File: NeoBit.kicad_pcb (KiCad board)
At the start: 2 copper layers, 67.3 x 45.7 mm, 13 parts, among them J2 Barrel_Jack_MountingPin, J4 NeoPixels, J5 microbit_edge_connector, U1 74AHCT125, U2 MCP1702-3302E_TO92

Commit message: Wire things up.
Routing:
- net +3V3: track 0.00 -> 99.5 mm, vias 0 -> 1
- net Net-(R2-Pad1): track 0.00 -> 90.5 mm, vias 0 -> 2
- net /P2: track 0.00 -> 69.6 mm, vias 0 -> 1
- net /P0: track 0.00 -> 46.3 mm, vias 0 -> 2
- net /P1: track 0.00 -> 33.6 mm, vias 0 -> 1
- net +5V: track 0.00 -> 33.5 mm
- net Net-(C4-Pad1): track 0.00 -> 8.41 mm
- net Net-(J4-Pad1): track 0.00 -> 6.02 mm
- added copper zone on F.Cu, net +5V
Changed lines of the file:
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@@
     (thickness 1.6)
     (drawings 8)
-    (tracks 0)
+    (tracks 84)
     (zones 0)
     (modules 13)
@@
     (pad_to_mask_clearance 0)
     (aux_axis_origin 0 0)
-    (visible_elements FFFEF77F)
+    (visible_elements FFFEE77F)
     (pcbplotparams
       (layerselection 0x00030_80000001)
@@
   (gr_arc (start 121.285 127) (end 121.285 129.54) (angle 90) (layer Edge.Cuts) (width 0.15))
   (gr_arc (start 121.285 86.36) (end 118.745 86.36) (angle 90) (layer Edge.Cuts) (width 0.15))
+  (segment (start 140.335 114.3) (end 137.795 114.3) (width 0.508) (layer F.Cu) (net 1))
+  (segment (start 137.795 114.3) (end 136.525 115.57) (width 0.508) (layer F.Cu) (net 1))
+  (segment (start 149.86 113.03) (end 149.49401 113.39599) (width 0.508) (layer F.Cu) (net 1))
+  (segment (start 149.49401 113.39599) (end 149.49401 113.704453) (width 0.508) (layer F.Cu) (net 1))
+  (segment (start 148.898463 114.3) (end 141.46637 114.3) (width 0.508) (layer F.Cu) (net 1))
+  (segment (start 149.49401 113.704453) (end 148.898463 114.3) (width 0.508) (layer F.Cu) (net 1))
+  (segment (start 141.46637 114.3) (end 140.335 114.3) (width 0.508) (layer F.Cu) (net 1))
+  (segment (start 154.94 111.125) (end 150.507 111.125) (width 0.508) (layer F.Cu) (net 1))
+  (segment (start 150.507 111.125) (end 149.86 111.772) (width 0.508) (layer F.Cu) (net 1))
+  (segment (start 149.86 111.772) (end 149.86 113.03) (width 0.508) (layer F.Cu) (net 1))
+  (segment (start 166.37 111.76) (end 163.521922 111.76) (width 0.508) (layer F.Cu) (net 1))
+  (segment (start 163.521922 111.76) (end 162.067921 110.305999) (width 0.508) (layer F.Cu) (net 1))
+  (segment (start 162.067921 110.305999) (end 155.759001 110.305999) (width 0.508) (layer F.Cu) (net 1))
+  (segment (start 155.759001 110.305999) (end 155.739999 110.325001) (width 0.508) (layer F.Cu) (net 1))
+  (segment (start 155.739999 110.325001) (end 154.94 111.125) (width 0.508) (layer F.Cu) (net 1))
+  (segment (start 144.78 111.125) (end 144.78 107.315) (width 0.508) (layer B.Cu) (net 3))
+  (segment (start 148.59 113.03) (end 146.685 113.03) (width 0.508) (layer F.Cu) (net 3))
+  (segment (start 146.685 113.03) (end 144.78 111.125) (width 0.508) (layer F.Cu) (net 3))
+  (segment (start 179.15 121.92) (end 183.609001 117.460999) (width 0.508) (layer B.Cu) (net 4))
+  (segment (start 183.609001 117.460999) (end 183.609001 106.089923) (width 0.508) (layer B.Cu) (net 4))
+  (segment (start 183.609001 106.089923) (end 179.15 101.630922) (width 0.508) (layer B.Cu) (net 4))
+  (segment (start 179.15 101.630922) (end 179.15 99.345634) (width 0.508) (layer B.Cu) (net 4))
+  (segment (start 179.15 99.345634) (end 179.15 97.79) (width 0.508) (layer B.Cu) (net 4))
+  (segment (start 157.48 121.92) (end 179.15 121.92) (width 0.508) (layer F.Cu) (net 4))
+  (segment (start 154.94 107.315) (end 154.94 109.023) (width 0.508) (layer B.Cu) (net 4))
+  (segment (start 154.94 109.023) (end 157.48 111.563) (width 0.508) (layer B.Cu) (net 4))
+  (segment (start 157.48 111.563) (end 157.48 121.92) (width 0.508) (layer B.Cu) (net 4))
+  (via (at 157.48 121.92) (size 0.6) (drill 0.4) (layers F.Cu B.Cu) (net 4))
+  (segment (start 160.02 91.44) (end 162.56 91.44) (width 0.508) (layer F.Cu) (net 4))
+  (segment (start 157.48 91.44) (end 160.02 91.44) (width 0.508) (layer F.Cu) (net 4))
+  (segment (start 158.75 89.54) (end 161.29 89.54) (width 0.508) (layer F.Cu) (net 4))
+  (segment (start 156.21 89.54) (end 158.75 89.54) (width 0.508) (layer F.Cu) (net 4))
+  (segment (start 162.56 91.44) (end 162.56 90.81) (width 0.508) (layer B.Cu) (net 4))
+  (segment (start 162.56 90.81) (end 161.29 89.54) (width 0.508) (layer B.Cu) (net 4))
+  (segment (start 160.02 91.44) (end 160.02 90.81) (width 0.508) (layer B.Cu) (net 4))
+  (segment (start 160.02 90.81) (end 158.75 89.54) (width 0.508) (layer B.Cu) (net 4))
+  (segment (start 157.48 91.44) (end 157.48 90.81) (width 0.508) (layer B.Cu) (net 4))
+  (segment (start 157.48 90.81) (end 156.21 89.54) (width 0.508) (layer B.Cu) (net 4))
+  (segment (start 154.94 107.315) (end 154.94 93.98) (width 0.508) (layer B.Cu) (net 4))
+  (segment (start 154.94 93.98) (end 157.48 91.44) (width 0.508) (layer B.Cu) (net 4))
+  (segment (start 124.46 91.44) (end 127 91.44) (width 0.25) (layer F.Cu) (net 5))
+  (segment (start 125.73 89.54) (end 128.27 89.54) (width 0.25) (layer F.Cu) (net 5))
+  (segment (start 127 91.44) (end 127 90.81) (width 0.25) (layer B.Cu) (net 5))
+  (segment (start 127 90.81) (end 128.27 89.54) (width 0.25) (layer B.Cu) (net 5))
+  (segment (start 124.46 91.44) (end 124.46 90.81) (width 0.25) (layer B.Cu) (net 5))
+  (segment (start 124.46 90.81) (end 125.73 89.54) (width 0.25) (layer B.Cu) (net 5))
+  (segment (start 133.985 111.76) (end 133.985 107.95) (width 0.25) (layer B.Cu) (net 5))
+  (segment (start 122.555 111.76) (end 133.985 111.76) (width 0.25) (layer F.Cu) (net 5))
+  (via (at 133.985 111.76) (size 0.6) (drill 0.4) (layers F.Cu B.Cu) (net 5))
+  (segment (start 124.46 91.44) (end 122.555 93.345) (width 0.25) (layer B.Cu) (net 5))
+  (segment (start 122.555 93.345) (end 122.555 96.305998) (width 0.25) (layer B.Cu) (net 5))
+  (segment (start 122.555 96.305998) (end 122.555 111.76) (width 0.25) (layer B.Cu) (net 5))
+  (via (at 122.555 111.76) (size 0.6) (drill 0.4) (layers F.Cu B.Cu) (net 5))
+  (segment (start 134.62 91.44) (end 137.16 91.44) (width 0.25) (layer F.Cu) (net 6))
+  (segment (start 135.89 89.54) (end 138.43 89.54) (width 0.25) (layer F.Cu) (net 6))
+  (segment (start 137.16 91.44) (end 137.16 90.81) (width 0.25) (layer B.Cu) (net 6))
+  (segment (start 137.16 90.81) (end 138.43 89.54) (width 0.25) (layer B.Cu) (net 6))
+  (segment (start 134.62 91.44) (end 134.62 90.81) (width 0.25) (layer B.Cu) (net 6))
+  (segment (start 134.62 90.81) (end 135.89 89.54) (width 0.25) (layer B.Cu) (net 6))
+  (segment (start 134.62 100.965) (end 134.62 91.44) (width 0.25) (layer B.Cu) (net 6))
+  (segment (start 120.65 101.29) (end 134.295 101.29) (width 0.25) (layer F.Cu) (net 6))
+  (segment (start 134.295 101.29) (end 134.62 100.965) (width 0.25) (layer F.Cu) (net 6))
+  (via (at 134.62 100.965) (size 0.6) (drill 0.4) (layers F.Cu B.Cu) (net 6))
+  (segment (start 147.32 91.44) (end 149.86 91.44) (width 0.25) (layer F.Cu) (net 7))
+  (segment (start 146.05 89.54) (end 148.59 89.54) (width 0.25) (layer F.Cu) (net 7))
+  (segment (start 149.86 91.44) (end 149.86 90.81) (width 0.25) (layer B.Cu) (net 7))
+  (segment (start 149.86 90.81) (end 148.59 89.54) (width 0.25) (layer B.Cu) (net 7))
+  (segment (start 147.32 91.44) (end 147.32 90.81) (width 0.25) (layer B.Cu) (net 7))
+  (segment (start 147.32 90.81) (end 146.05 89.54) (width 0.25) (layer B.Cu) (net 7))
+  (segment (start 147.32 123.825) (end 147.32 91.44) (width 0.25) (layer B.Cu) (net 7))
+  (segment (start 120.65 125.42) (end 122.245 123.825) (width 0.25) (layer F.Cu) (net 7))
+  (segment (start 122.245 123.825) (end 147.32 123.825) (width 0.25) (layer F.Cu) (net 7))
+  (via (at 147.32 123.825) (size 0.6) (drill 0.4) (layers F.Cu B.Cu) (net 7))
+  (segment (start 184.188012 104.813012) (end 184.188012 123.786988) (width 0.25) (layer B.Cu) (net 48))
+  (segment (start 182.88 103.505) (end 184.188012 104.813012) (width 0.25) (layer B.Cu) (net 48))
+  (segment (start 183.179999 124.795001) (end 182.88 125.095) (width 0.25) (layer B.Cu) (net 48))
+  (segment (start 184.188012 123.786988) (end 183.179999 124.795001) (width 0.25) (layer B.Cu) (net 48))
+  (segment (start 132.715 125.095) (end 132.715 109.22) (width 0.25) (layer B.Cu) (net 48))
+  (segment (start 132.715 109.22) (end 131.445 107.95) (width 0.25) (layer B.Cu) (net 48))
+  (segment (start 182.88 125.095) (end 132.715 125.095) (width 0.25) (layer F.Cu) (net 48))
+  (via (at 132.715 125.095) (size 0.6) (drill 0.4) (layers F.Cu B.Cu) (net 48))
+  (via (at 182.88 125.095) (size 0.6) (drill 0.4) (layers F.Cu B.Cu) (net 48))
+  (segment (start 182.88 95.885) (end 179.07 92.075) (width 0.25) (layer B.Cu) (net 52))
+  (segment (start 179.07 92.075) (end 179.07 91.44) (width 0.25) (layer B.Cu) (net 52))
+  (zone (net 1) (net_name +5V) (layer F.Cu) (hatch edge 0.508)
+    (priority 1)
+    (connect_pads (clearance 0.3048))
+    (min_thickness 0.254)
+    (fill (arc_segments 16) (thermal_gap 0.508) (thermal_bridge_width 0.508))
+    (polygon
+      (pts
+        (xy 181.61 85.725) (xy 181.61 115.57) (xy 163.83 115.57) (xy 163.83 95.25) (xy 173.99 85.725)
+      )
+    )
+  )
 )

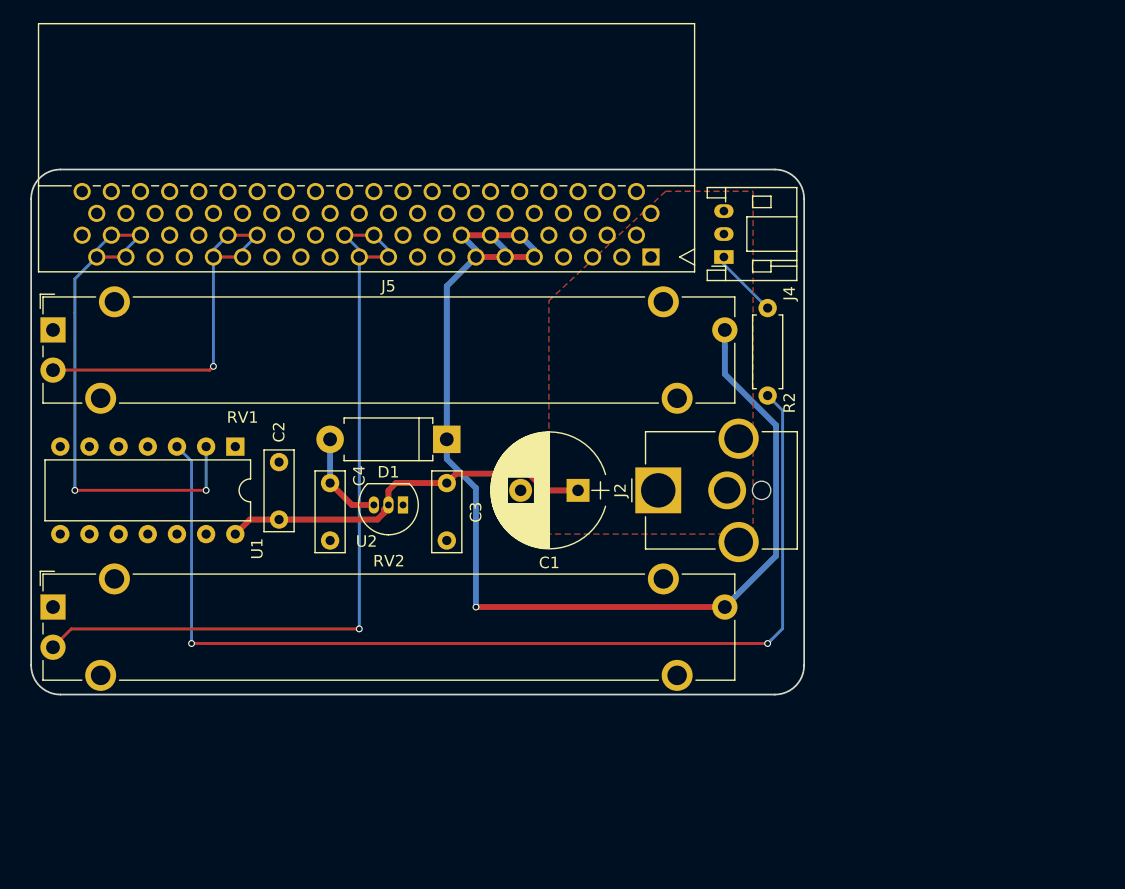
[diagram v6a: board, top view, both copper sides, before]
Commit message: Fill zones.
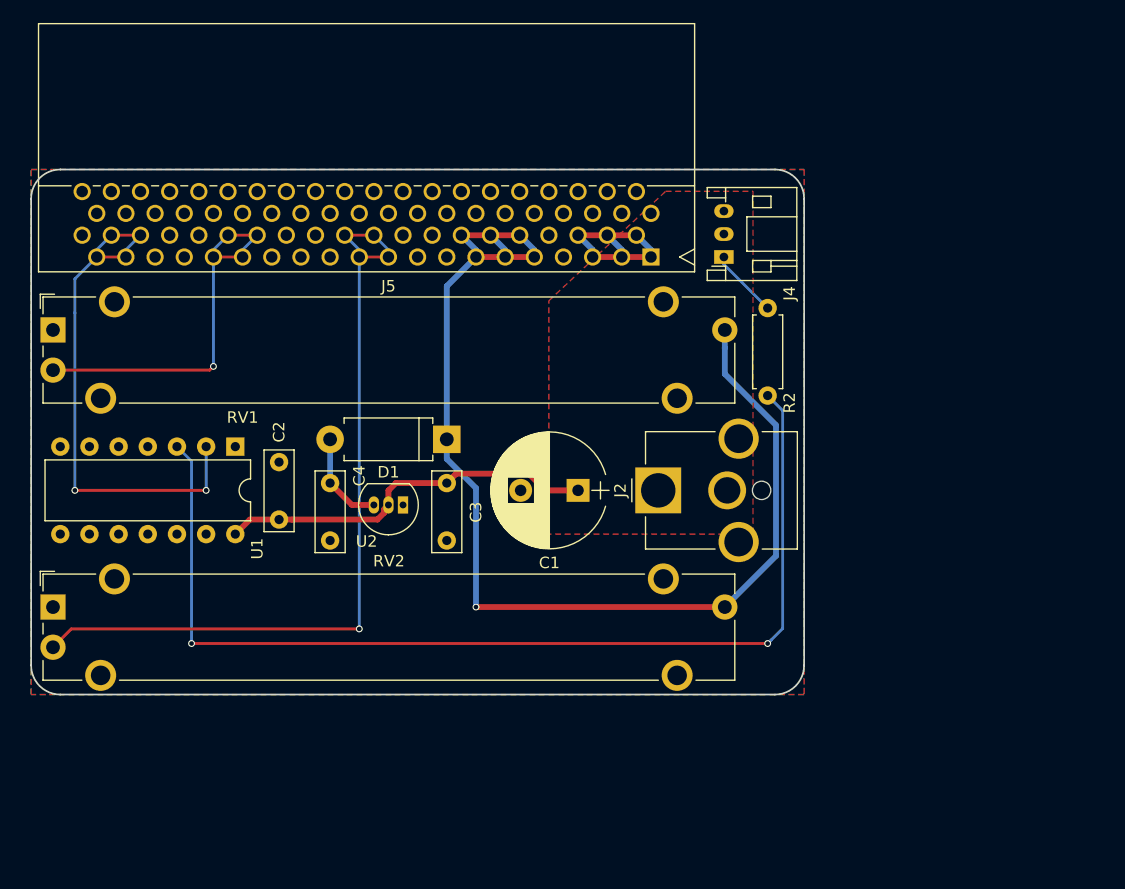
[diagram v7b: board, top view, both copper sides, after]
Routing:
- net GND: track 0.00 -> 17.4 mm
- added copper zone on B.Cu, net GND
- added copper zone on F.Cu, net GND
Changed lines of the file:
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@@
   (general
     (links 62)
-    (no_connects 62)
-    (area 0 0 0 0)
+    (no_connects 0)
+    (area 117.98 69.015 187.43 130.495)
     (thickness 1.6)
     (drawings 8)
-    (tracks 84)
+    (tracks 94)
     (zones 0)
     (modules 13)
@@
   )
   (setup
-    (last_trace_width 0.25)
+    (last_trace_width 0.508)
     (user_trace_width 0.508)
     (user_trace_width 1.016)
@@
     (pad_to_mask_clearance 0)
     (aux_axis_origin 0 0)
-    (visible_elements FFFEE77F)
+    (visible_elements FFFEF77F)
     (pcbplotparams
       (layerselection 0x00030_80000001)
@@
   (segment (start 155.759001 110.305999) (end 155.739999 110.325001) (width 0.508) (layer F.Cu) (net 1))
   (segment (start 155.739999 110.325001) (end 154.94 111.125) (width 0.508) (layer F.Cu) (net 1))
+  (segment (start 170.18 91.44) (end 172.72 91.44) (width 0.508) (layer F.Cu) (net 2))
+  (segment (start 167.64 91.44) (end 170.18 91.44) (width 0.508) (layer F.Cu) (net 2))
+  (segment (start 168.91 89.54) (end 171.45 89.54) (width 0.508) (layer F.Cu) (net 2))
+  (segment (start 166.37 89.54) (end 168.91 89.54) (width 0.508) (layer F.Cu) (net 2))
+  (segment (start 167.64 91.44) (end 167.64 90.81) (width 0.508) (layer B.Cu) (net 2))
+  (segment (start 167.64 90.81) (end 166.37 89.54) (width 0.508) (layer B.Cu) (net 2))
+  (segment (start 170.18 91.44) (end 170.18 90.81) (width 0.508) (layer B.Cu) (net 2))
+  (segment (start 170.18 90.81) (end 168.91 89.54) (width 0.508) (layer B.Cu) (net 2))
+  (segment (start 172.72 91.44) (end 172.72 90.81) (width 0.508) (layer B.Cu) (net 2))
+  (segment (start 172.72 90.81) (end 171.45 89.54) (width 0.508) (layer B.Cu) (net 2))
   (segment (start 144.78 111.125) (end 144.78 107.315) (width 0.508) (layer B.Cu) (net 3))
   (segment (start 148.59 113.03) (end 146.685 113.03) (width 0.508) (layer F.Cu) (net 3))
@@
     (connect_pads (clearance 0.3048))
     (min_thickness 0.254)
-    (fill (arc_segments 16) (thermal_gap 0.508) (thermal_bridge_width 0.508))
+    (fill yes (arc_segments 16) (thermal_gap 0.508) (thermal_bridge_width 0.508))
     (polygon
       (pts
@@
       )
     )
+  )
+  (zone (net 2) (net_name GND) (layer F.Cu) (hatch edge 0.508)
+    (connect_pads (clearance 0.3048))
+    (min_thickness 0.254)
+    (fill yes (arc_segments 16) (thermal_gap 0.508) (thermal_bridge_width 0.508))
+    (polygon
+      (pts
+        (xy 186.055 129.54) (xy 118.745 129.54) (xy 118.745 83.82) (xy 186.055 83.82)
+      )
+    )
+  )
+  (zone (net 2) (net_name GND) (layer B.Cu) (hatch edge 0.508)
+    (connect_pads (clearance 0.3048))
+    (min_thickness 0.254)
+    (fill yes (arc_segments 16) (thermal_gap 0.508) (thermal_bridge_width 0.508))
+    (polygon
+      (pts
+        (xy 186.055 129.54) (xy 118.745 129.54) (xy 118.745 83.82) (xy 186.055 83.82)
+      )
+    )

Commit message: Add stuff on back silkscreen.
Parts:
- added G***: LOGO, footprints:Fingerprint, B.Cu at (165.1, 121.9)
- added REF***: OSHW-Symbol_6.7x6mm_SilkScreen, Symbols:OSHW-Symbol_6.7x6mm_SilkScreen, B.Cu at (139.7, 121.9)
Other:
- board text added: "2018-09-03 https://github.com/ppelleti/NeoBit designed by Patrick Pelletier"
